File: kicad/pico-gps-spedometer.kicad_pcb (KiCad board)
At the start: 2 copper layers, 89 x 76 mm, 30 parts, among them J1 Akkumulátor be, J2 TP4056-18650-Charger, J3 uBlox NEO GPS (6M/8M), Q1 PN2222A, Q2 BC212, U1 RP2040-ZERO, U2 DS18B20, U3 LM7805_TO220, U4 TFT_320x240

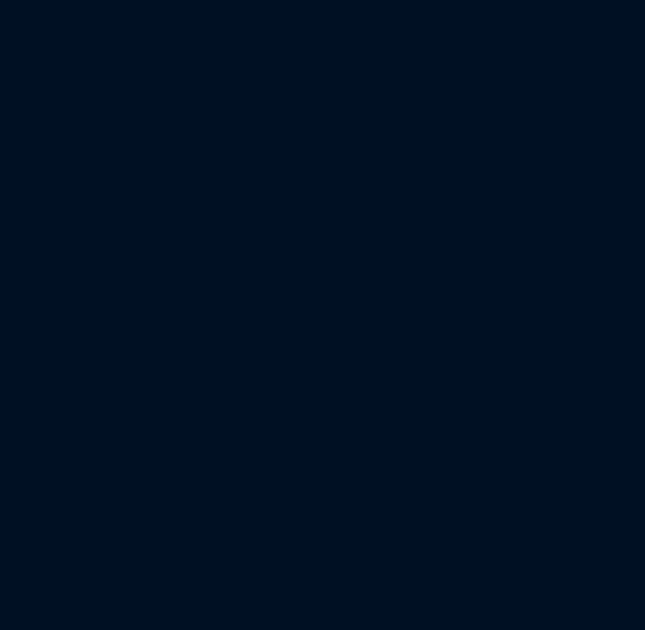
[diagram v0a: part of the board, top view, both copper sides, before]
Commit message: Refactor voltage measurement and update schematic
- Updated the schematic to add a new junction and reposition existing junctions for better clarity.
- Modified the voltage measurement logic in ScreenMain to differentiate between VBus and VSys based on the externalVoltageMode flag.
- Enhanced the demo data generation to simulate both VBus and VSys values.
- Added a touch event handler to toggle between voltage modes when interacting with the voltage bar.
- Introduced a new method in SensorUtils to read the external VSYS voltage using a voltage divider.
- Removed unnecessary build flags from platformio.ini for cleaner configuration.
- Added a new resistor component to the schematic for improved circuit design.
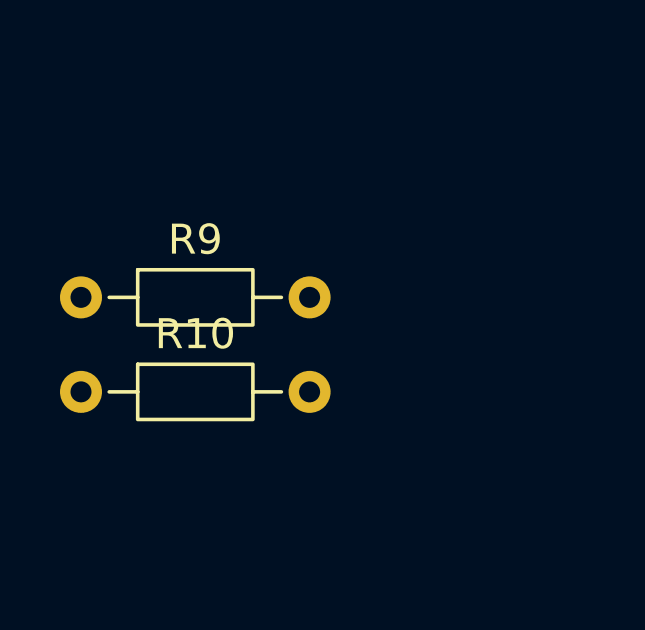
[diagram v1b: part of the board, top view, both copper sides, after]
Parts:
- added R10: 10k, Resistor_THT:R_Axial_DIN0204_L3.6mm_D1.6mm_P7.62mm_Horizontal, F.Cu at (31.9, 46.8)
- added R9: 4k7, Resistor_THT:R_Axial_DIN0204_L3.6mm_D1.6mm_P7.62mm_Horizontal, F.Cu at (31.9, 43.6)
- Q2: value BC212 -> PN2222A
- R7: value 390 -> 510
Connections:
- U1 pad 19: unconnected-(U1-GP28-Pad19) -> Net-(U1-GP28)
- U4 pad 9: /MISO -> unconnected-(U4-SDO/MISO-Pad9)
